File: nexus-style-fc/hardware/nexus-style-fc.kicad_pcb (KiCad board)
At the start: 6 copper layers, 22.4 x 33.1 mm, 89 parts, among them J1 Header child board, J2 DSM (UART1), J3 A-CRSF (UART4), J4 C (UART3), J5 B (UART6), J6 USB-C vertical, SW1 BOOT, U1 STM32F722RET6, U10 TPS70933DBVR, U11 SRV05-4, U12 SRV05-4, U13 SRV05-4, U14 TPS629210DRLR, U15 SRV05-4, U2 ICM-42688-P, U3 DPS368XTSA1, U4 W25N01GVZEIG, U5 TPS62130RGTR, U7 USBLC6-2SC6, U9 TPS2116DRLR, Y1 8MHz 20pF

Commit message: fixed dfm warnings
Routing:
- net A_TX: track 15.5 -> 12.8 mm
- net GND: track 202.3 -> 202.9 mm
- net NRST: track 44.6 -> 45.2 mm
- net 5V: track 83.5 -> 84.0 mm

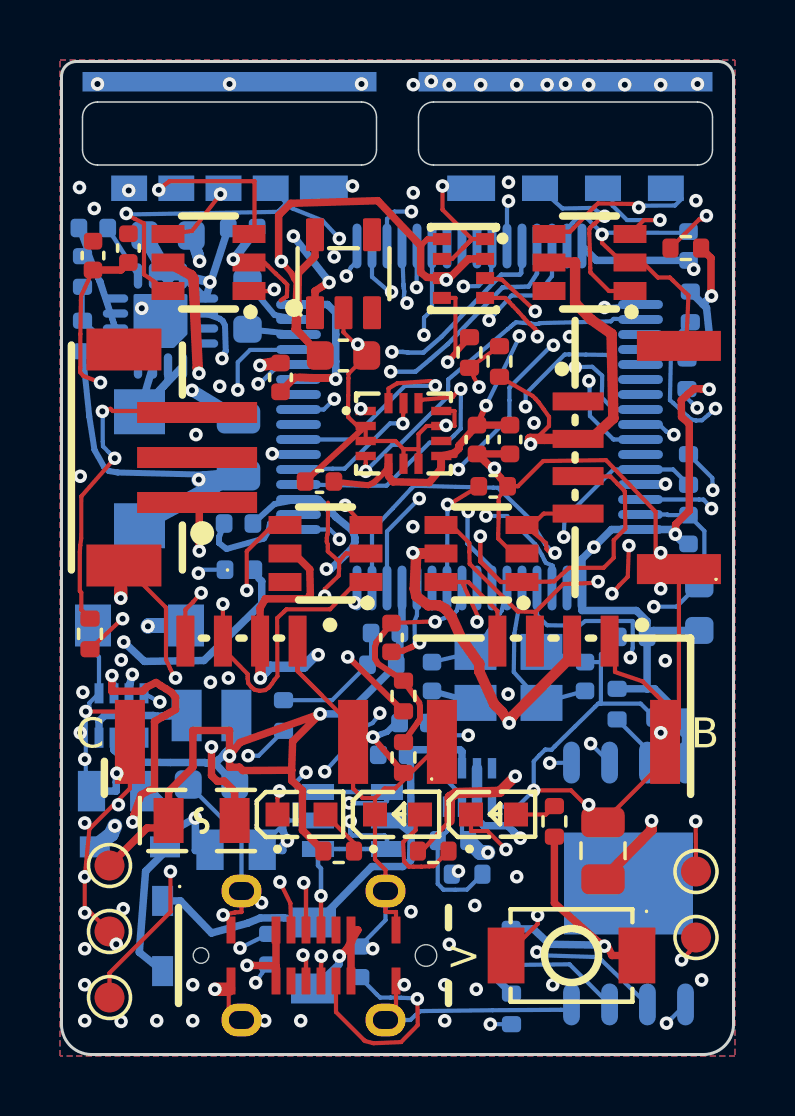
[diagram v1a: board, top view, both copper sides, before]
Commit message: fixed dfm errors and updated vx path
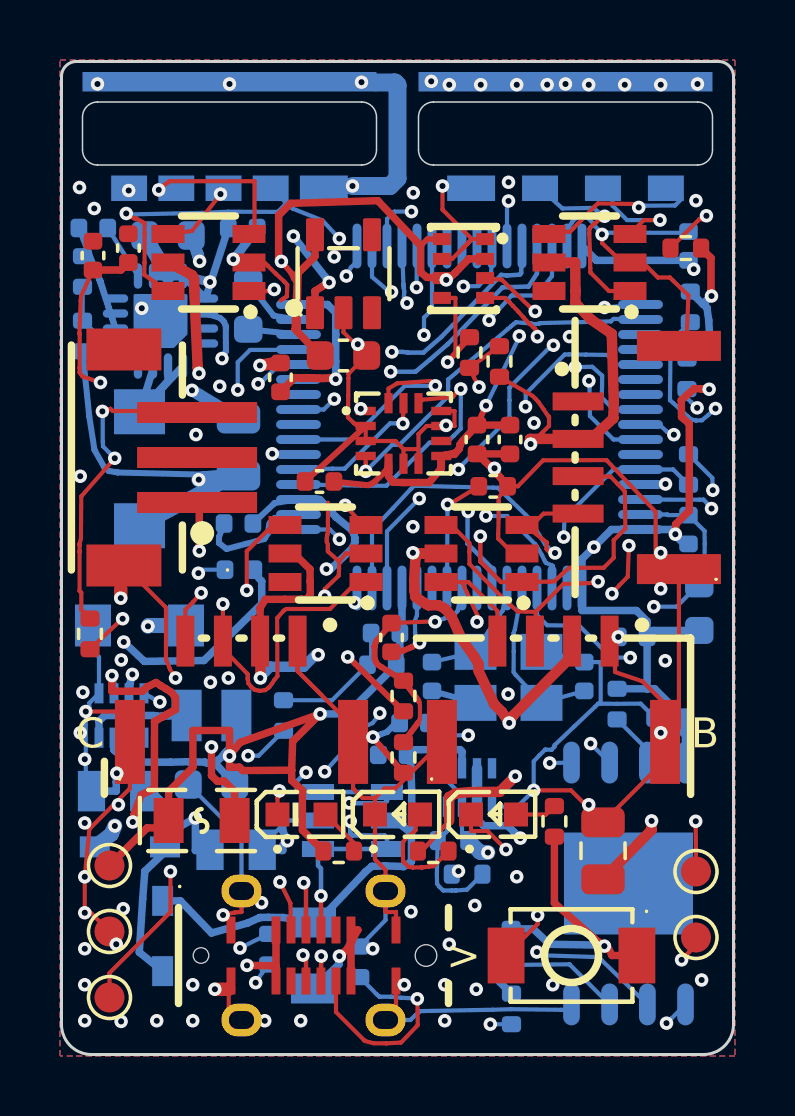
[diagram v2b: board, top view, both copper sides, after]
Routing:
- net VX: track 96.4 -> 89.5 mm
- net GND: track 202.9 -> 202.0 mm
- net LED2_K: track 18.3 -> 17.4 mm

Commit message: USB rerouted for 90ohm
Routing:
- net USB_DP: track 35.6 -> 37.8 mm

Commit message: updated bom
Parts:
- added R23: 0.12, NexusFC:R_0402_1005Metric__VCAP_Dense, B.Cu at (106.2, 108.6)
- C9: footprint Capacitor_SMD:C_0603_1608Metric -> NexusFC:C_0402_1005Metric__VCAP_Dense
- D4: value SMF13A -> SMF9.0A; footprint NexusFC:SOD-123FL_L2.8-W1.8-LS3.6-RD -> NexusFC:SOD-123FL_L2.8-W1.8-LS3.6-RD__Littelfuse_SMF9
- moved C9 1.22 mm to (106.2, 106.9)
- moved C31 0.07 mm to (105.8, 126.2)
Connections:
- C9 pad 1: VCAP -> VCAP_C
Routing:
- net DSM_TX: track 41.9 -> 40.2 mm
- net 5V_BUCK: track 41.8 -> 43.3 mm
- net IMU_CS: track 28.4 -> 27.5 mm
- net VCAP_C: track 0.00 -> 0.72 mm
- net LED1_K: track 27.1 -> 26.5 mm
- net GND: track 202.0 -> 202.5 mm, vias 78 -> 79
